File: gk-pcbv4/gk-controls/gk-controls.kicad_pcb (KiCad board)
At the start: 2 copper layers, 101.6 x 76.2 mm, 88 parts, among them J1 Conn_01x20, U1 PCAL6416APW, U2 ULN2003A

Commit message: update ground fills
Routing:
- net BTN_MCU_D: track 41.1 -> 40.3 mm
- net BTN_MCU_R: track 30.0 -> 30.7 mm
- net BTN_MCU_L: track 34.1 -> 33.5 mm
- net BTN_MCU_U: track 47.0 -> 46.4 mm

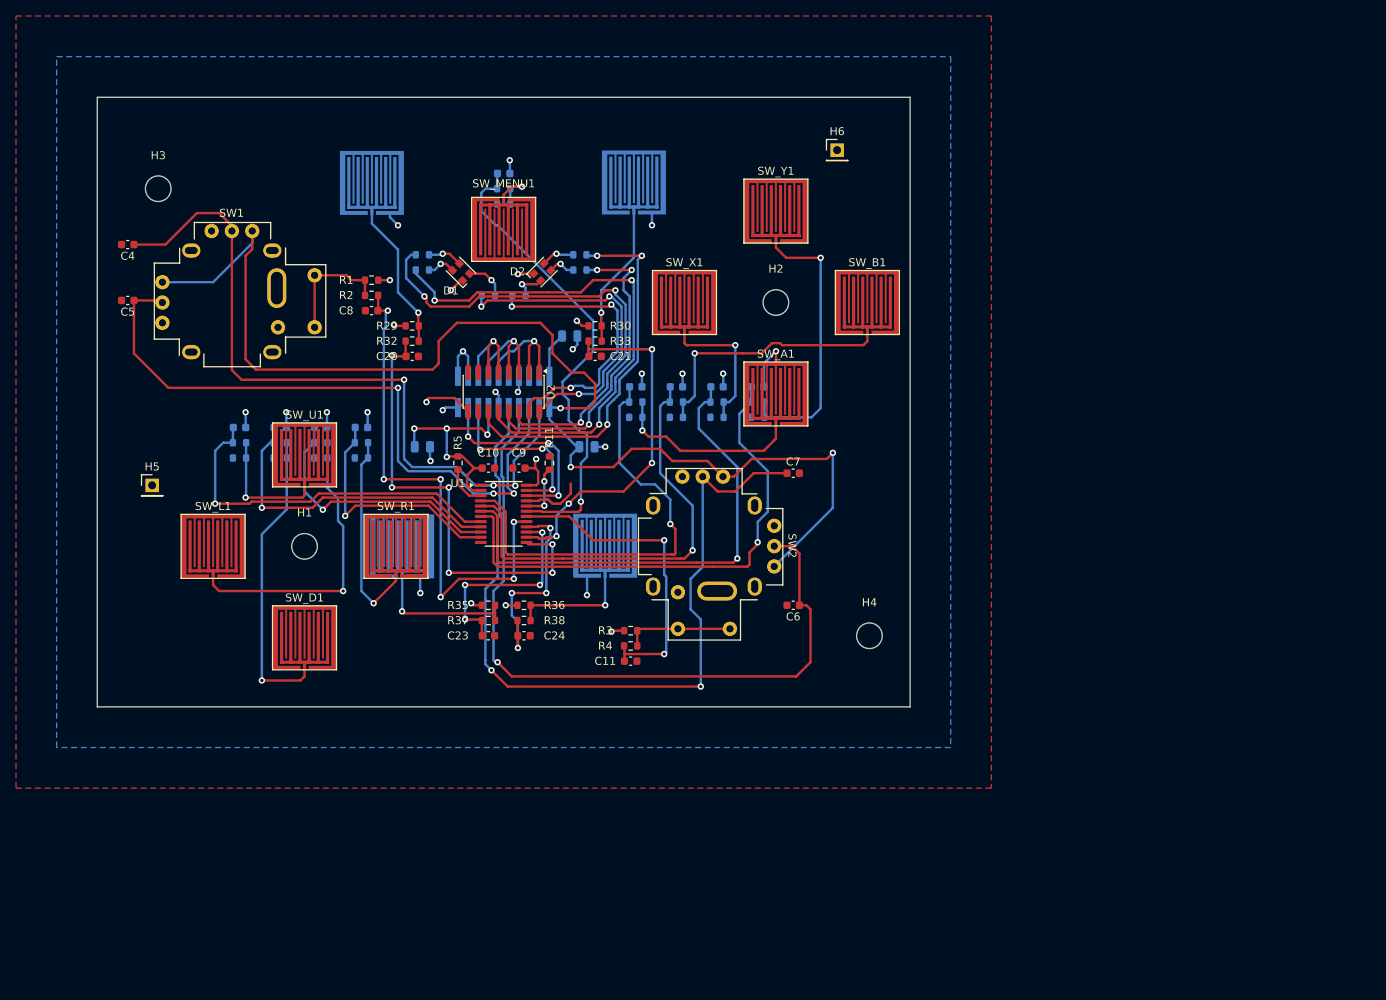
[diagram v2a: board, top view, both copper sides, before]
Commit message: add v2 controls board
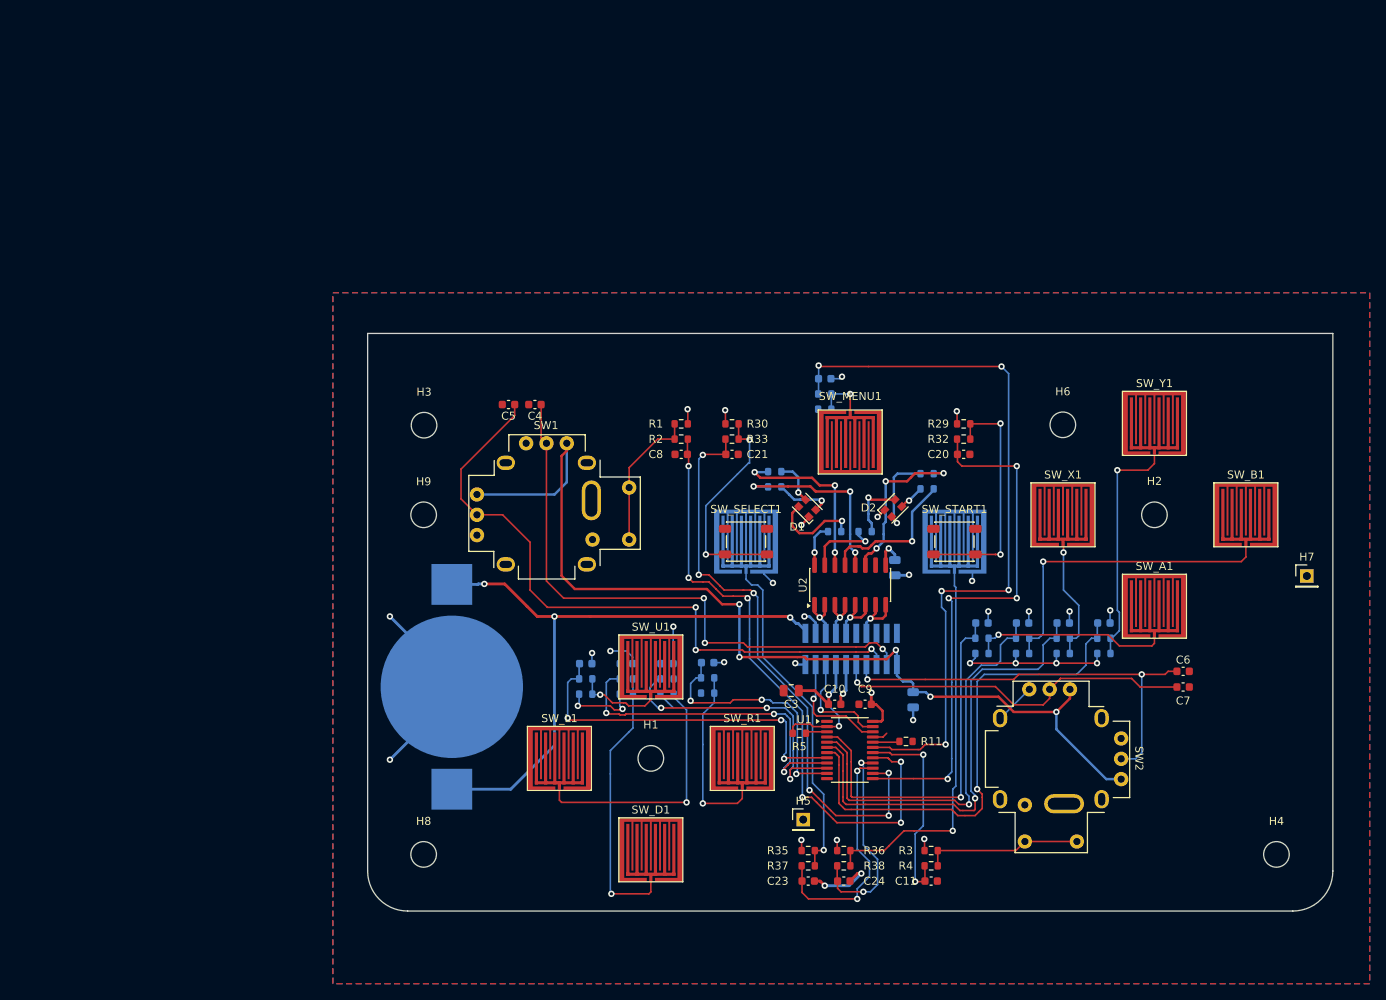
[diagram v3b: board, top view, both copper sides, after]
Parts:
- removed SW_LB1, SW_RB1: SW_Push, gk:TouchButton-8x8mm_2
- added BT1: Battery_Cell, Battery:BatteryHolder_Keystone_3002_1x2032, B.Cu at (100.2, 104.2)
- added H7: Conn_01x01, Connector_PinHeader_2.54mm:PinHeader_1x01_P2.54mm_Vertical, F.Cu at (207.1, 90.3)
- added H8: MountingHole, MountingHole:MountingHole_3.2mm_M3, F.Cu at (96.7, 125.1)
- added H9: MountingHole, MountingHole:MountingHole_3.2mm_M3, F.Cu at (96.7, 82.7)
- added SW_SELECT1: SW_Push, Button_Switch_SMD:SW_SPST_PTS647_Sx38, F.Cu at (137.0, 86.0)
- added SW_START1: SW_Push, Button_Switch_SMD:SW_SPST_PTS647_Sx38, F.Cu at (163.0, 86.0)
- C3: moved to F.Cu
- H6: value Conn_01x01 -> MountingHole; footprint Connector_PinHeader_2.54mm:PinHeader_1x01_P2.54mm_Vertical -> MountingHole:MountingHole_3.2mm_M3
- moved H5 91.5 mm to (144.1, 120.8)
- moved C20 70.0 mm to (164.2, 75.1)
- moved R29 70.0 mm to (164.2, 71.3)
- moved R32 70.0 mm to (164.2, 73.2)
- moved H4 57.8 mm to (203.3, 125.1)
- moved R11 56.6 mm to (157.0, 111.0), turned to 0 degrees
- moved C7 55.6 mm to (191.6, 104.2)
- moved C3 55.3 mm to (142.6, 104.6), turned to 180 degrees
- moved C4 54.7 mm to (110.6, 68.9)
- moved R5 54.4 mm to (143.6, 110.0), turned to 0 degrees
- moved SW_B1 54.2 mm to (199.5, 82.7)
- moved H2 54.2 mm to (188.0, 82.7)
- moved SW_A1 54.2 mm to (188.0, 94.1)
- moved SW_X1 54.2 mm to (176.6, 82.7)
- moved SW_Y1 54.2 mm to (188.0, 71.2)
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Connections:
- net BTN_MCU_LB renamed BTN_MCU_START
- net BTN_MCU_RB renamed BTN_MCU_SELECT
- net ROT_A renamed Net-(R21-Pad2)
- net ROT_B renamed Net-(R22-Pad2)
- J1 pad 20: GND -> Net-(BT1-+)
- J1 pad 4: I2C4_SDA_3V3 -> unconnected-(J1-Pin_4-Pad4)
- J1 pad 6: I2C4_SCL_3V3 -> unconnected-(J1-Pin_6-Pad6)
- R12 pad 1: Net-(D2-BK) -> Net-(D2-RK)
- R6 pad 1: Net-(D1-RK) -> Net-(D1-BK)
- R8 pad 1: Net-(D1-BK) -> Net-(D1-RK)
- R9 pad 1: Net-(D2-RK) -> Net-(D2-BK)
- U2 pad 1: BTNLED_R -> BTNLED_B
- U2 pad 2: BTNLED_R -> BTNLED_B
- U2 pad 5: BTNLED_B -> BTNLED_R
- U2 pad 6: BTNLED_B -> BTNLED_R
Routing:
- net Net-(BT1-+): track 0.00 -> 78.3 mm, vias 0 -> 3
- net JOY_B_Y: track 101.4 -> 45.9 mm, vias 2 -> 1
- net Net-(U2-O5): track 65.0 -> 23.6 mm
- net JOY_B_X: track 92.5 -> 53.7 mm, vias 1 -> 2
- net Net-(U2-O3): track 61.1 -> 22.4 mm
- net Net-(U2-O1): track 40.2 -> 5.47 mm, vias 3 -> 1
- net Net-(R36-Pad2): track 15.2 -> 48.6 mm
- net BTN_MCU_MENU: track 60.0 -> 92.1 mm, vias 1 -> 5
- net VDDA: track 155.5 -> 126.1 mm, vias 3 -> 5
- net BTN_MCU_SELECT: track 45.3 -> 73.9 mm, vias 4 -> 6
- net GND: track 54.6 -> 82.1 mm, vias 20 -> 21
- net Net-(U2-O6): track 47.6 -> 20.7 mm
- net Net-(U2-O2): track 36.2 -> 9.33 mm, vias 3 -> 1
- net Net-(R35-Pad2): track 18.3 -> 42.6 mm
- net +3V3: track 31.3 -> 54.5 mm, vias 10 -> 16
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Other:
- board size 101.6 x 76.2 mm -> 120.6 x 72.2 mm

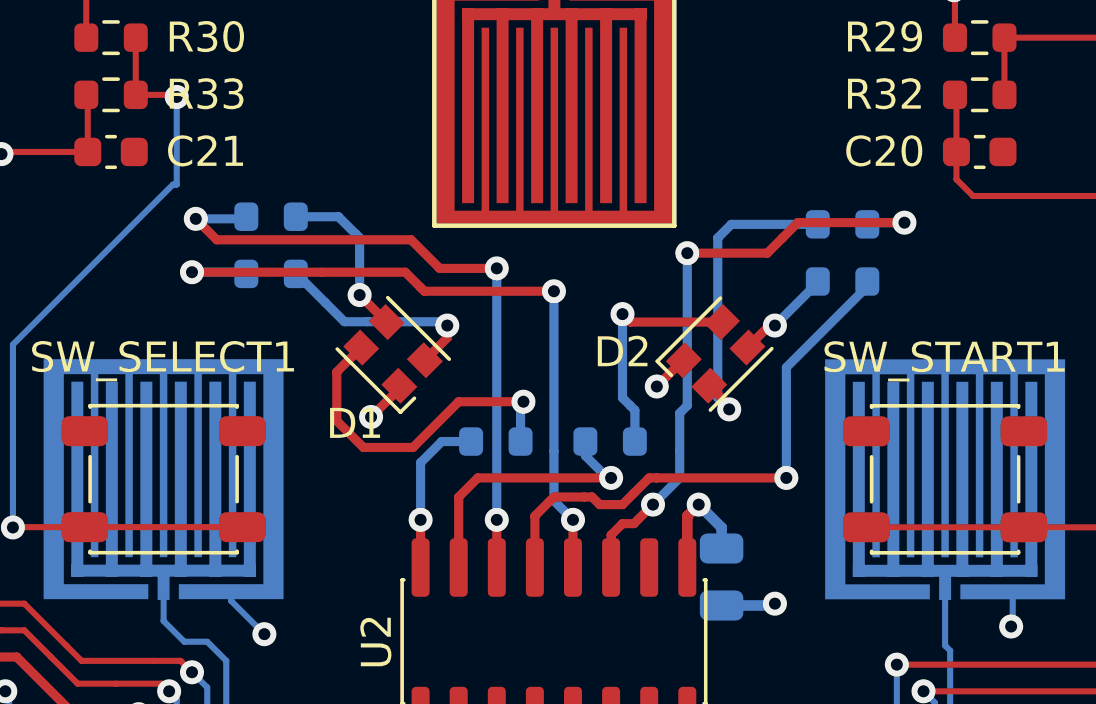
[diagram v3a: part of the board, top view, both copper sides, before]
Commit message: nudge btnleds up to the appropriate spot
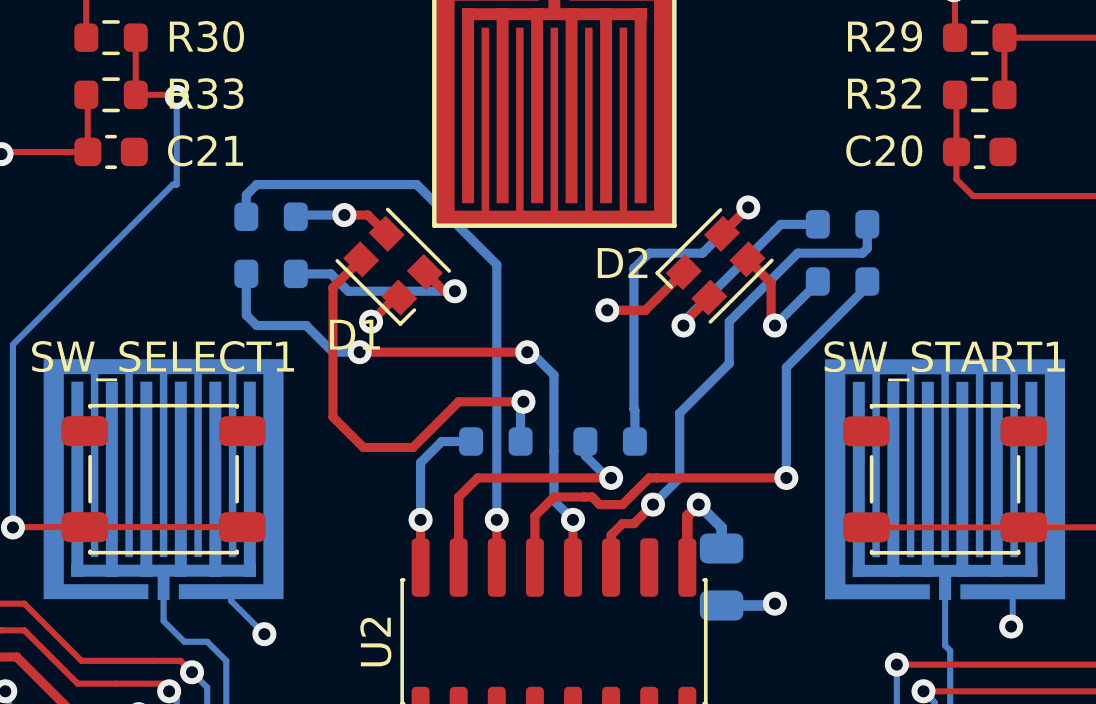
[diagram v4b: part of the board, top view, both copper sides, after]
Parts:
- moved D1 2.94 mm to (144.6, 78.9)
- moved D2 2.94 mm to (155.4, 78.9)
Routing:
- net Net-(U2-O5): track 23.6 -> 19.1 mm
- net Net-(U2-O6): track 20.7 -> 16.5 mm, vias 3 -> 1
- net Net-(D2-BK): track 7.84 -> 11.7 mm
- net Net-(D2-RK): track 10.5 -> 7.24 mm
- net Net-(D1-BK): track 11.4 -> 14.4 mm
- net Net-(D1-GK): track 5.60 -> 3.31 mm
- net Net-(U2-O3): track 22.4 -> 20.4 mm, vias 3 -> 1
- net +3V3: track 54.5 -> 56.2 mm
- net Net-(D2-GK): track 3.28 -> 4.65 mm

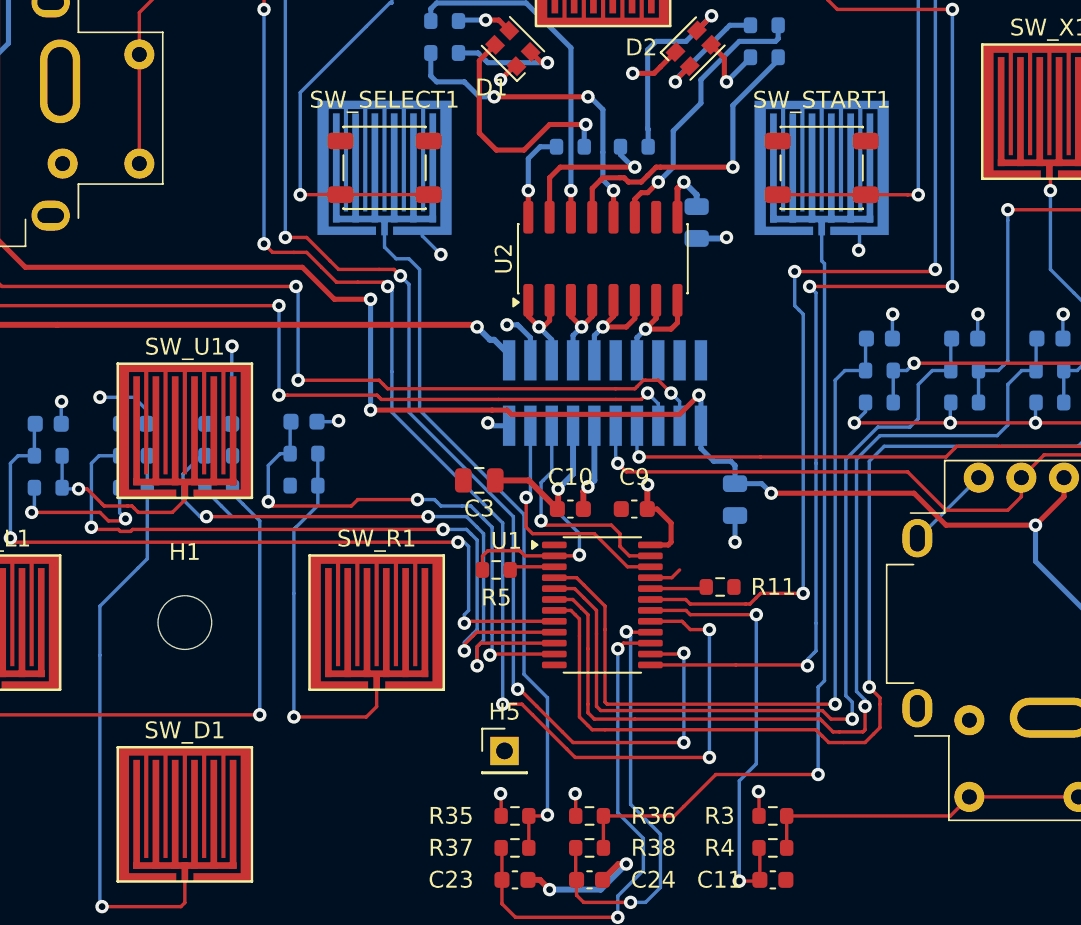
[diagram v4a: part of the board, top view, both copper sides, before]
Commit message: begin adding breakout board for triggers
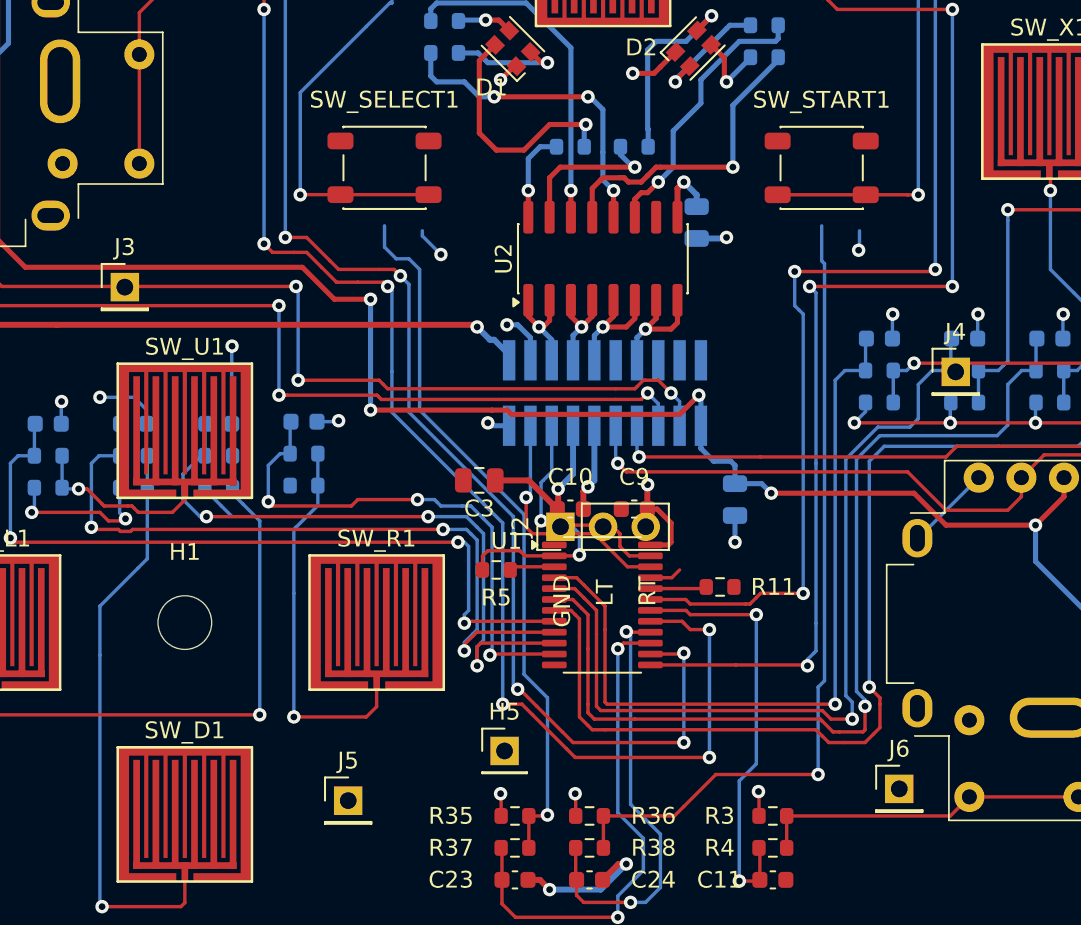
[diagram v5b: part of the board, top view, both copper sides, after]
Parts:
- removed SW_LT1, SW_RT1: SW_Push, gk:TouchButton-8x8mm_2
- added J2: Conn_01x03, Connector_PinHeader_2.54mm:PinHeader_1x03_P2.54mm_Vertical, F.Cu at (147.5, 107.4)
- added J3: Conn_01x01, Connector_PinHeader_2.54mm:PinHeader_1x01_P2.54mm_Vertical, F.Cu at (121.5, 93.1)
- added J4: Conn_01x01, Connector_PinHeader_2.54mm:PinHeader_1x01_P2.54mm_Vertical, F.Cu at (171.0, 98.2)
- added J5: Conn_01x01, Connector_PinHeader_2.54mm:PinHeader_1x01_P2.54mm_Vertical, F.Cu at (134.8, 123.7)
- added J6: Conn_01x01, Connector_PinHeader_2.54mm:PinHeader_1x01_P2.54mm_Vertical, F.Cu at (167.7, 123.0)
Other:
- board text added: "GND"
- board text added: "LT"
- board text added: "RT"
